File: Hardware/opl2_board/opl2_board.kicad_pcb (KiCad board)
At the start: 2 copper layers, 80.8 x 60.1 mm, 6 parts, among them J1 Conn_01x40

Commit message: opl2 board progress
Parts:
- added C1: C_Small, Capacitor_SMD:C_1206_3216Metric_Pad1.42x1.75mm_HandSolder, B.Cu at (27.5, -42.1)
- added C2: C_Small, Capacitor_SMD:C_1206_3216Metric_Pad1.42x1.75mm_HandSolder, B.Cu at (36.3, -28.4)
- added C3: C_Small, Capacitor_SMD:C_1206_3216Metric_Pad1.42x1.75mm_HandSolder, B.Cu at (22.4, -23.2)
- added C4: 10uF, Capacitor_SMD:C_1206_3216Metric_Pad1.42x1.75mm_HandSolder, F.Cu at (33.5, -51.1)
- added C5: 10uF, Capacitor_SMD:C_1206_3216Metric_Pad1.42x1.75mm_HandSolder, F.Cu at (29.5, -52.5)
- added C6: C_Small, Capacitor_SMD:C_1206_3216Metric_Pad1.42x1.75mm_HandSolder, B.Cu at (50.4, -45.4)
- added C7: C_Small, Capacitor_SMD:C_1206_3216Metric_Pad1.42x1.75mm_HandSolder, B.Cu at (49.7, -18.5)
- added D1: 1N4148, Diode_THT:D_DO-35_SOD27_P7.62mm_Horizontal, F.Cu at (51.1, -10.5)
- added D2: LED, LED_SMD:LED_1206_3216Metric_Pad1.42x1.75mm_HandSolder, F.Cu at (7.94, -43.8)
- added J2: AudioJack3, Connector_Audio:Jack_3.5mm_CUI_SJ1-3533NG_Horizontal, F.Cu at (75.2, -45.4)
- added R1: 1k, Resistor_SMD:R_0805_2012Metric_Pad1.15x1.40mm_HandSolder, F.Cu at (54.2, -10.5)
- added R2: 330R, Resistor_SMD:R_0805_2012Metric_Pad1.15x1.40mm_HandSolder, F.Cu at (7.49, -40.8)
- added U1: 74HC00, Package_DIP:DIP-14_W7.62mm_Socket, F.Cu at (23.8, -28.4)
- added U2: YM3812, Package_DIP:DIP-24_W15.24mm_Socket, F.Cu at (48.1, -16.3)
- added U3: YM3014B, Package_DIP:DIP-8_W7.62mm_Socket, F.Cu at (29.8, -40.6)
- added U4: LM358, Package_DIP:DIP-8_W7.62mm_Socket, F.Cu at (49.0, -40.1)
- added X1: CXO_DIP8, Oscillator:Oscillator_DIP-8, F.Cu at (34.8, -23.1)
- moved G*** 1.08 mm to (14.4, -55.2)
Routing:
- net R~W~: track 0.00 -> 66.3 mm, vias 0 -> 4
- net ~SLOT_SEL~: track 0.00 -> 61.7 mm
- net Net-(U1-Pad8): track 0.00 -> 58.4 mm, vias 0 -> 2
- net Net-(U1-Pad3): track 0.00 -> 47.1 mm, vias 0 -> 1
- net ~RESET~: track 0.00 -> 42.6 mm, vias 0 -> 1
- net ~SLOT_IRQ~: track 0.00 -> 37.8 mm, vias 0 -> 1
- net Net-(U2-Pad23): track 0.00 -> 33.7 mm, vias 0 -> 1
- net A0: track 0.00 -> 29.9 mm, vias 0 -> 1
- net D4: track 0.00 -> 29.7 mm
- net D5: track 0.00 -> 29.7 mm
- net D3: track 0.00 -> 29.7 mm
- net D7: track 0.00 -> 29.7 mm
- net D6: track 0.00 -> 29.7 mm
- net D2: track 0.00 -> 29.7 mm
- net Net-(C4-Pad1): track 0.00 -> 29.0 mm
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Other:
- board text added: "OPL2 BOARD V1.0"
- board text removed: "XXXXXXX BOARD V1.0"

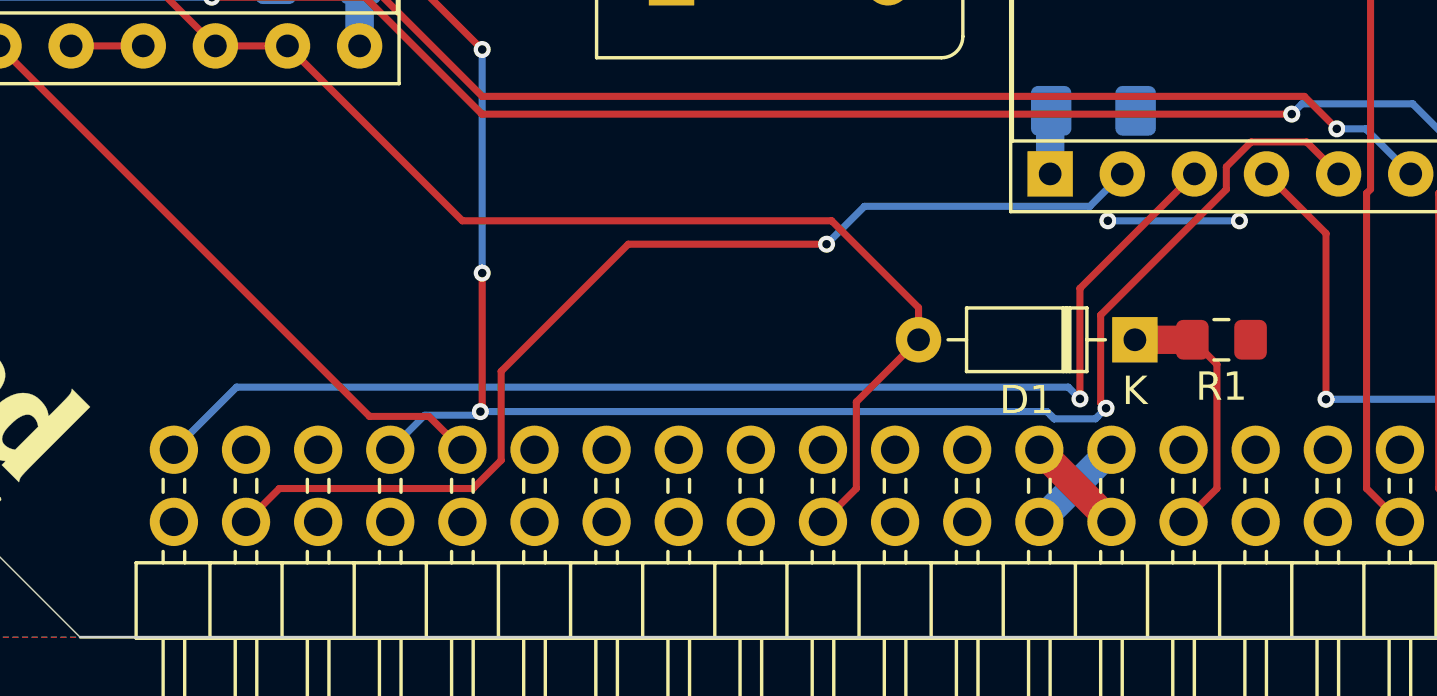
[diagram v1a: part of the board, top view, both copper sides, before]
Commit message: Backplane provides diode and pullups for SLOW signal
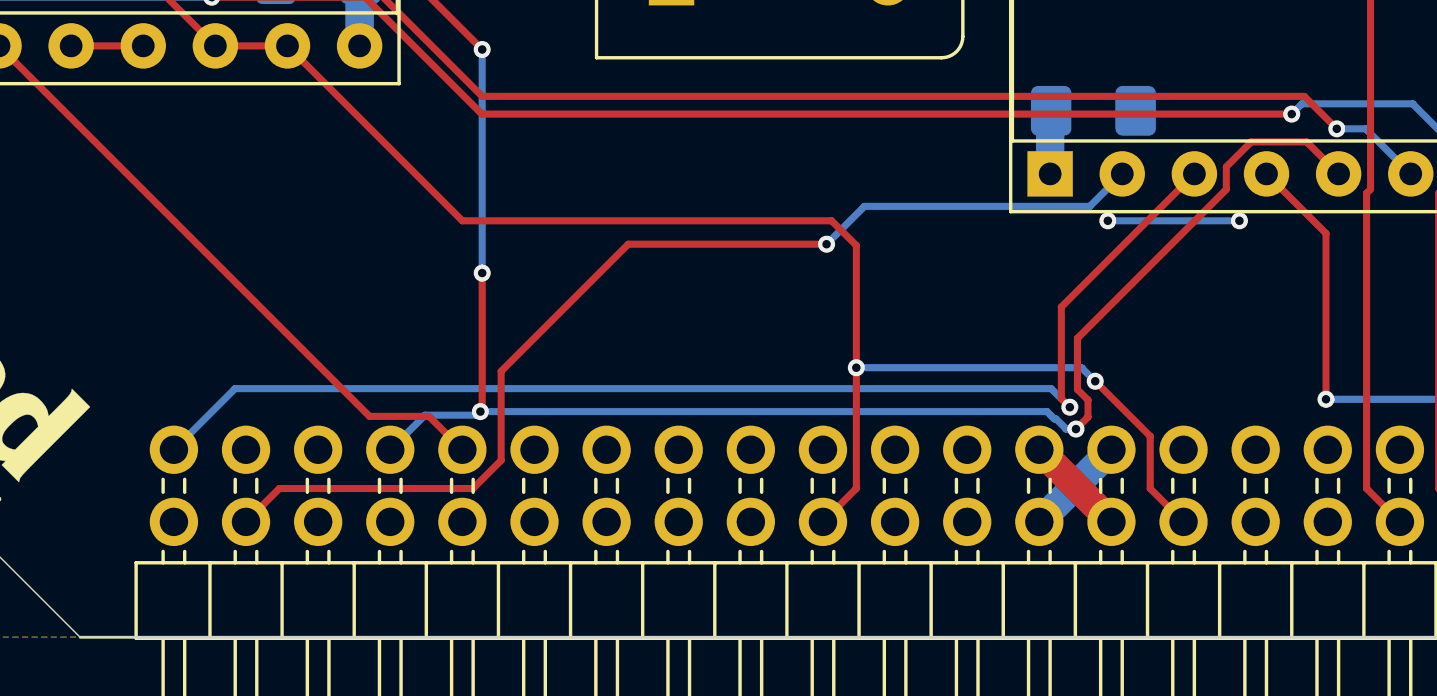
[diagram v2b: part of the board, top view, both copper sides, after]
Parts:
- removed D1: 1N4148, Diode_THT:D_DO-35_SOD27_P7.62mm_Horizontal
- removed R1: 1k, Resistor_SMD:R_0805_2012Metric_Pad1.15x1.40mm_HandSolder
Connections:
- J1 pad 22: ~SLOW~ -> ~SLOT_SEL~
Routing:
- net ~SLOT_SEL~: track 61.7 -> 74.7 mm, vias 0 -> 2
- net ~SLOW~: track 9.28 -> 0.00 mm
